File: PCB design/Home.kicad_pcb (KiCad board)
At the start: 2 copper layers, 121.9 x 157.5 mm, 17 parts, among them J1 Fan, J2 LCD, J3 EM LOCK, J4 ACS712 Signal, J5 Power In, J7 RFID, J8 RFID, J9 LCD, U1 ACS712, U3 DHT11, U5 PIR, U6 MQ2

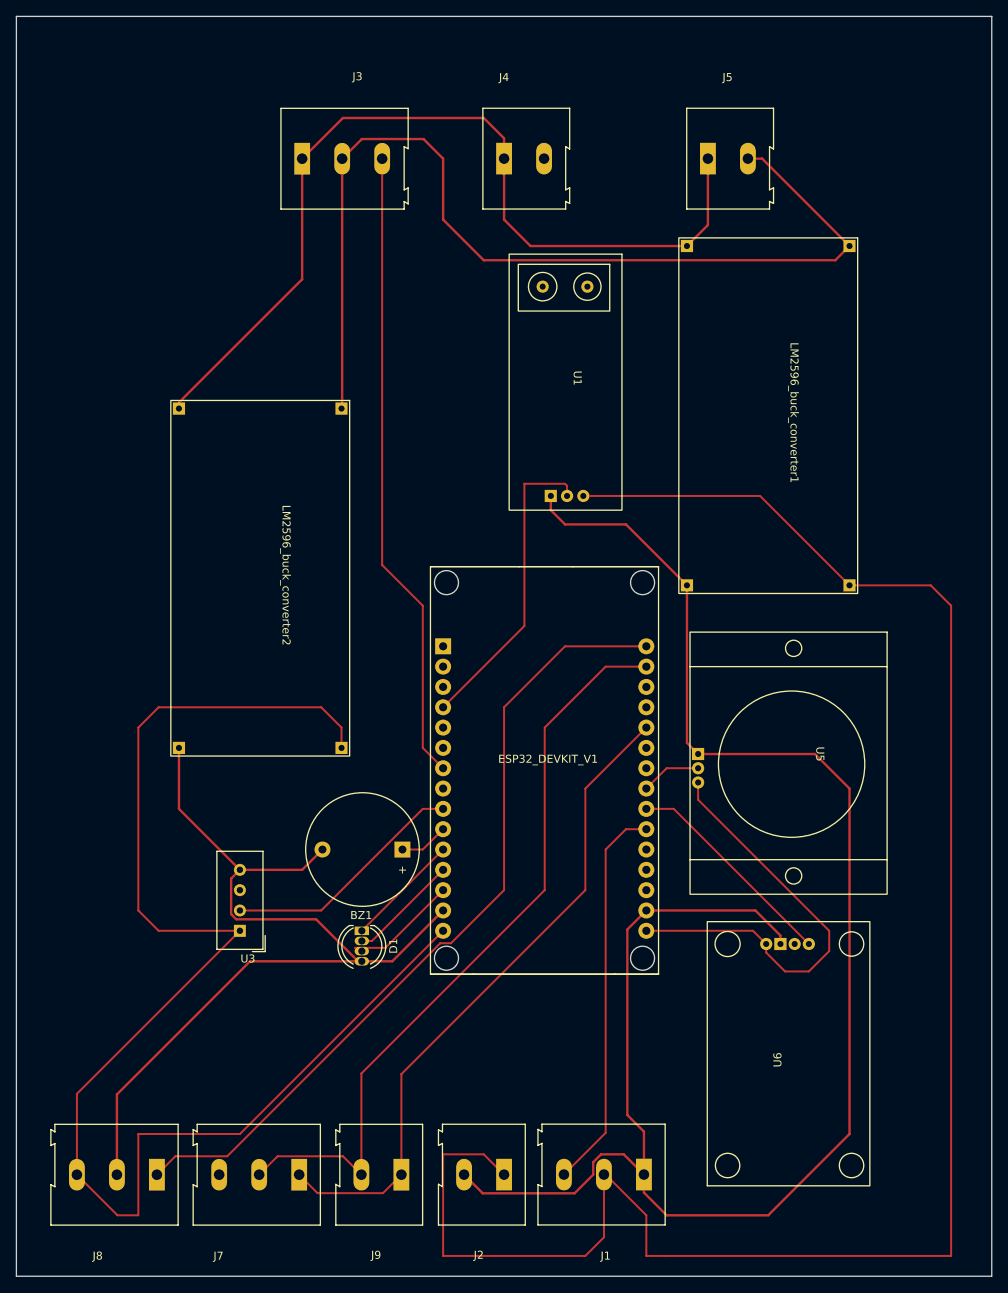
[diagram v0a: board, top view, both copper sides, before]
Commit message: added relay
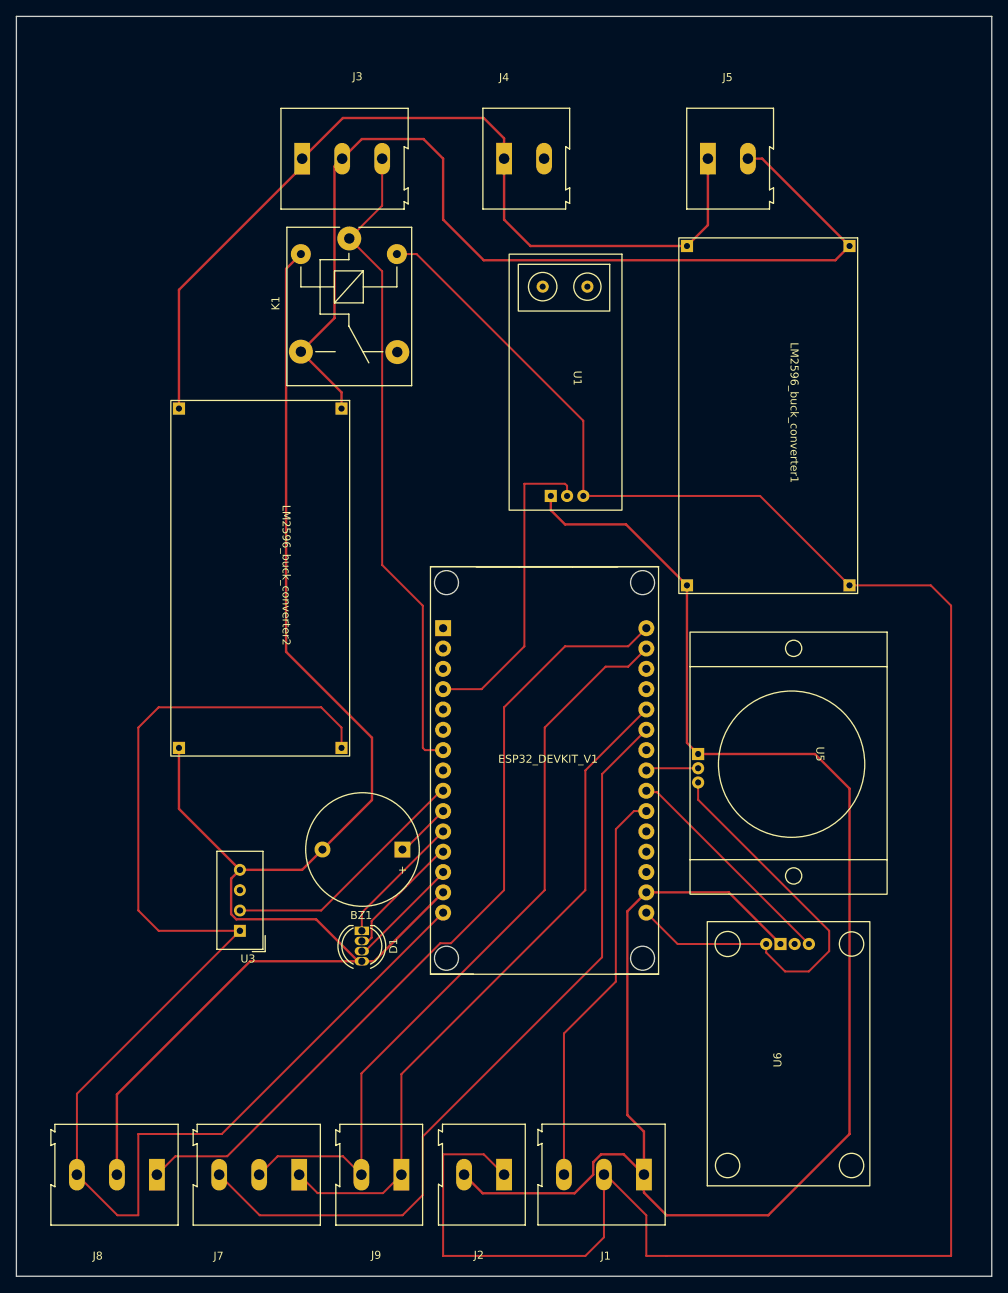
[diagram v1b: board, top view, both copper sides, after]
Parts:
- added K1: SANYOU_SRD_Form_C, Relay_THT:Relay_SPDT_SANYOU_SRD_Series_Form_C, F.Cu at (89.9, 45.5)
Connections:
- J7 pad 3: unconnected-(J7-Pin_3-Pad3) -> MISO
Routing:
- net MISO: track 0.00 -> 98.3 mm
- net GND: track 337.9 -> 423.6 mm
- net +5V: track 233.8 -> 275.1 mm
- net +12V: track 124.4 -> 128.6 mm
- net RELAY: track 79.3 -> 81.8 mm
- net RED: track 14.4 -> 16.6 mm
- net SDA: track 83.3 -> 85.5 mm
- net BLUE: track 13.8 -> 16.0 mm
- net Fan: track 48.9 -> 50.6 mm
- net +3.3V: track 174.1 -> 175.1 mm
- net PIR: track 7.53 -> 6.59 mm
- net DHT: track 30.7 -> 31.6 mm
- net BUZZ: track 6.13 -> 7.07 mm
- net SCK: track 95.9 -> 96.9 mm
- net MOSI: track 101.9 -> 102.9 mm
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
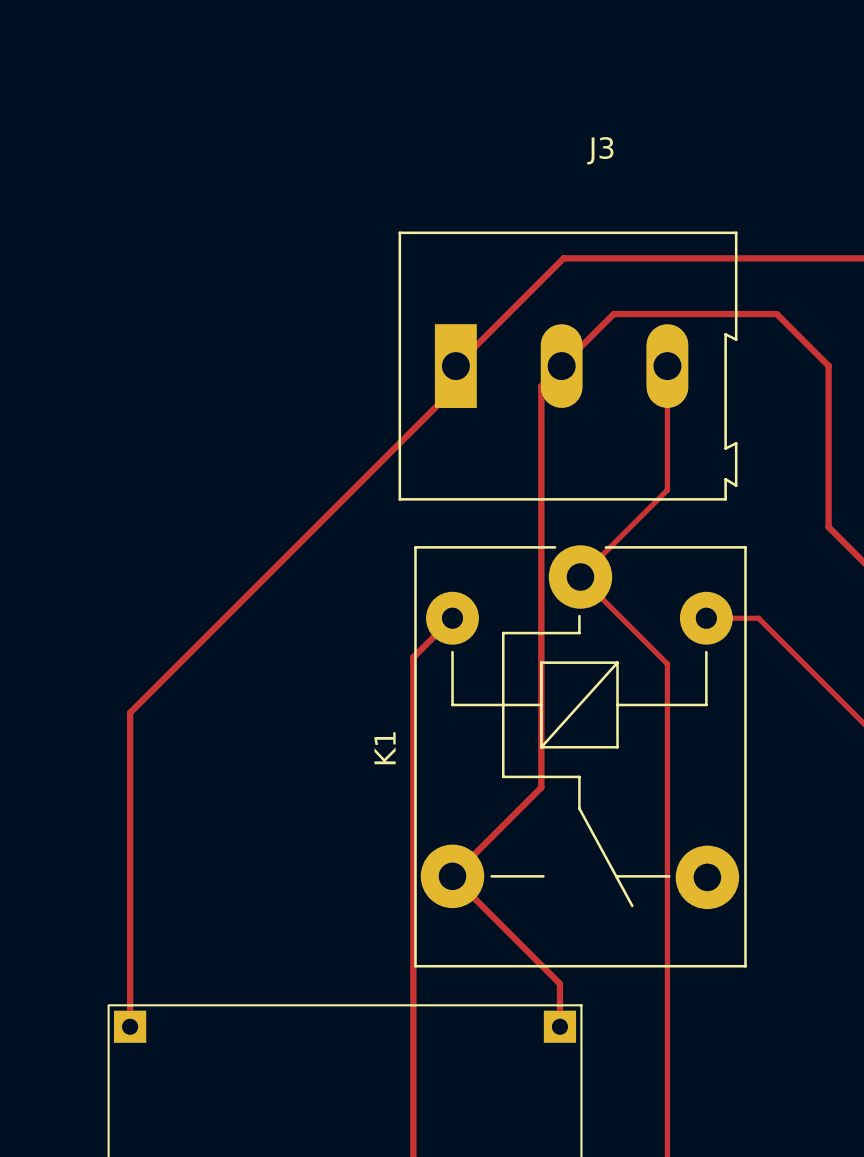
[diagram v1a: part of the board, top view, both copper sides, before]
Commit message: edited relay
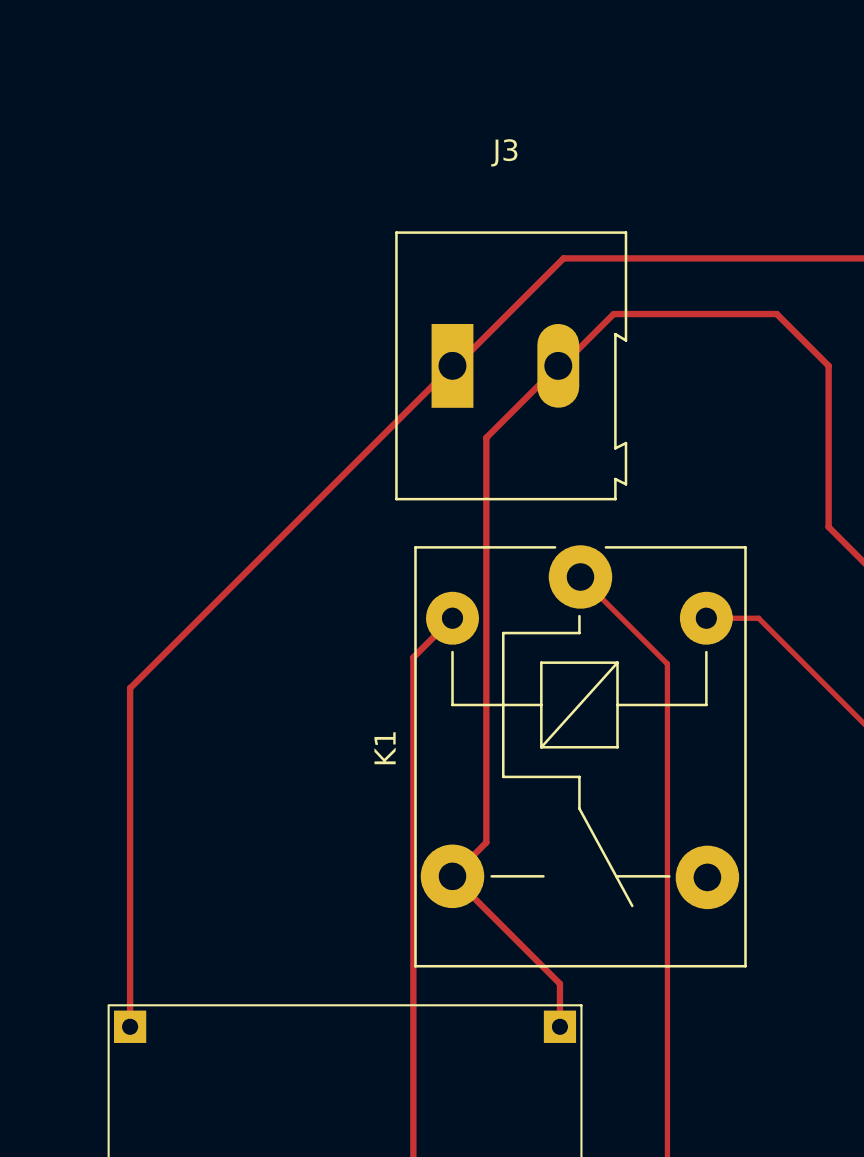
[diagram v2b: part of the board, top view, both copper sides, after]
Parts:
- J3: value EM LOCK -> EM lock; footprint TerminalBlock:TerminalBlock_Altech_AK300-3_P5.00mm -> TerminalBlock:TerminalBlock_Altech_AK300-2_P5.00mm
- moved J3 0.16 mm to (83.8, 35.6)
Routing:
- net RELAY: track 81.8 -> 70.1 mm
- net +12V: track 128.6 -> 130.1 mm
- net -12V: track 112.4 -> 113.3 mm

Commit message: Readme updated
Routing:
- net +5V: track 275.1 -> 270.6 mm
- net +3.3V: track 175.1 -> 172.4 mm
- net GND: track 423.6 -> 421.7 mm
- net ACS: track 39.4 -> 38.3 mm
- net +12V: track 130.1 -> 129.2 mm
- net SCK: track 96.9 -> 96.2 mm
- net 3V3: track 55.2 -> 54.6 mm
- net MISO: track 98.3 -> 97.7 mm
- net -12V: track 113.3 -> 112.8 mm

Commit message: 3D
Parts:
- moved U6 16.1 mm to (134.1, 147.8)
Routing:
- net 3V3: track 54.6 -> 80.2 mm
- net +3.3V: track 172.4 -> 159.9 mm
- net GND: track 421.7 -> 433.7 mm
- net MQ2: track 28.2 -> 39.4 mm
- net -12V: track 112.8 -> 115.5 mm
